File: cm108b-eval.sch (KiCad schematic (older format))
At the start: 42 parts, among them IC1 CM108B, J1 SPKR, J2 MIC, J3 RADIO_DATA, SW1 MUTE_REC, SW2 MUTE_PLAY, SW3 VOL_DN, SW4 VOL_UP

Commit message: Fix USB connector from A to micro-B
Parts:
- JP2: value USB_A -> USB_MICRO_B; symbol Connector:USB_A -> Connector:USB_B_Micro
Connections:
- net GND: now also JP2.5 (GND); no longer JP2.4 (GND)
- net at L2.2: now also JP2.6 (Shield); no longer JP2.5 (Shield)
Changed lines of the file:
@@
 $EndComp
 $Comp
-L Connector:USB_A JP2
+L Connector:USB_B_Micro JP2
 U 1 1 6057963A
 P 1350 2850
 F 0 "JP2" H 1407 3317 50  0000 C CNN
-F 1 "USB_A" H 1407 3226 50  0000 C CNN
+F 1 "USB_MICRO_B" H 1407 3226 50  0000 C CNN
 F 2 "Connector_USB:USB_Micro-B_Molex_47346-0001" H 1500 2800 50  0001 C CNN
 F 3 "https://www.mouser.com/datasheet/2/276/0473460001_IO_CONNECTORS-229243.pdf" H 1500 2800 50  0001 C CNN

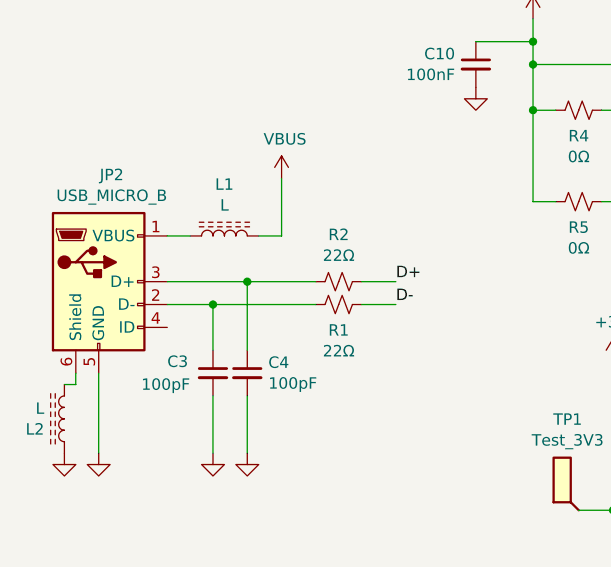
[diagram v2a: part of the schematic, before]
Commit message: Update micro USB part, and clean up libraries
The Molex micro USB is nearly impossible to hand solder, so I'm moving to the CUI
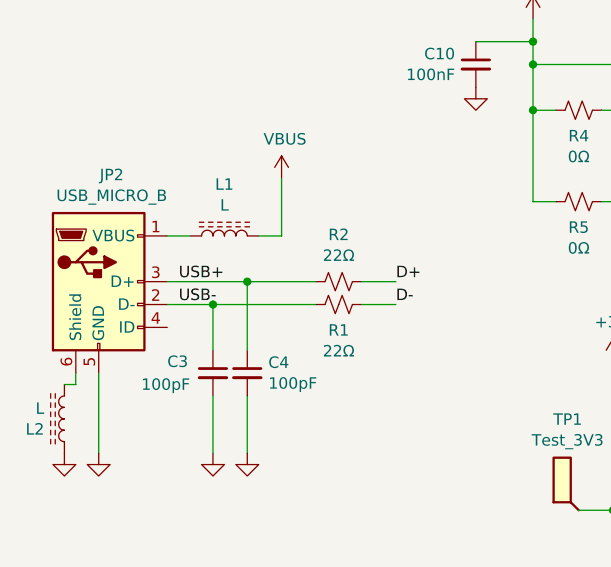
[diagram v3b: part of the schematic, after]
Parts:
- JP2: footprint Connector_USB:USB_Micro-B_Molex_47346-0001 -> CUI:UJ2-MIBH-4-SMT; Price 0.95 -> 0.79; Vendor Part # 538-47346-0001 -> 490-UJ2-MIBH-4-SMT
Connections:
- net USB-: now reaches C3.1, JP2.2 (D-), R1.2
- net USB+: now reaches C4.1, JP2.3 (D+), R2.2
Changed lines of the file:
@@
 Sheet 1 1
 Title "CM108B Evaluation Board"
-Date "2021-04-05"
-Rev "3"
+Date "2021-04-14"
+Rev "4"
 Comp "Chris Keller"
 Comment1 ""
@@
 NoConn ~ 4050 5150
 $Comp
-L power:GND #PWR?
+L power:GND #PWR0102
 U 1 1 605F61ED
 P 1350 3600
-F 0 "#PWR?" H 1350 3350 50  0001 C CNN
+F 0 "#PWR0102" H 1350 3350 50  0001 C CNN
 F 1 "GND" H 1355 3427 50  0001 C CNN
 F 2 "" H 1350 3600 50  0001 C CNN
@@
 F 0 "JP2" H 1407 3317 50  0000 C CNN
 F 1 "USB_MICRO_B" H 1407 3226 50  0000 C CNN
-F 2 "Connector_USB:USB_Micro-B_Molex_47346-0001" H 1500 2800 50  0001 C CNN
-F 3 "https://www.mouser.com/datasheet/2/276/0473460001_IO_CONNECTORS-229243.pdf" H 1500 2800 50  0001 C CNN
-F 4 "0.95" H 1407 3417 50  0001 C CNN "Price"
-F 5 "538-47346-0001" H 1407 3417 50  0001 C CNN "Vendor Part #"
+F 2 "CUI:UJ2-MIBH-4-SMT" H 1500 2800 50  0001 C CNN
+F 3 "https://www.mouser.com/datasheet/2/670/uj2_mibh_4_smt-1313358.pdf" H 1500 2800 50  0001 C CNN
+F 4 "0.79" H 1407 3417 50  0001 C CNN "Price"
+F 5 "490-UJ2-MIBH-4-SMT" H 1407 3417 50  0001 C CNN "Vendor Part #"
 F 6 "Mouser" H 1407 3417 50  0001 C CNN "Vendor"
 	1    1350 2850
@@
 Wire Wire Line
 	1250 3300 1200 3300
+Text Label 1700 2850 0    50   ~ 0
+USB+
+Text Label 1700 2950 0    50   ~ 0
+USB-
 $EndSCHEMATC

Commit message: Update BOM
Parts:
- R4: Vendor Part # 661-RK73Z2ETTD -> 660-RK73Z2ETTD
- R5: Vendor Part # 662-RK73Z2ETTD -> 660-RK73Z2ETTD
- R6: Vendor Part # 663-RK73Z2ETTD -> 660-RK73Z2ETTD
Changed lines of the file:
@@
 F 3 "https://www.mouser.com/datasheet/2/219/RK73Z-1825387.pdf" H 3450 2100 50  0001 C CNN
 F 4 "0.14" H 3563 2200 50  0001 C CNN "Price"
-F 5 "661-RK73Z2ETTD" H 3563 2200 50  0001 C CNN "Vendor Part #"
+F 5 "660-RK73Z2ETTD" H 3563 2200 50  0001 C CNN "Vendor Part #"
 F 6 "Mouser" H 3563 2200 50  0001 C CNN "Vendor"
 	1    3450 2100
@@
 F 3 "https://www.mouser.com/datasheet/2/219/RK73Z-1825387.pdf" H 3450 2500 50  0001 C CNN
 F 4 "0.14" H 3563 2600 50  0001 C CNN "Price"
-F 5 "662-RK73Z2ETTD" H 3563 2600 50  0001 C CNN "Vendor Part #"
+F 5 "660-RK73Z2ETTD" H 3563 2600 50  0001 C CNN "Vendor Part #"
 F 6 "Mouser" H 3563 2600 50  0001 C CNN "Vendor"
 	1    3450 2500
@@
 F 3 "https://www.mouser.com/datasheet/2/219/RK73Z-1825387.pdf" H 8550 3250 50  0001 C CNN
 F 4 "0.14" H 8663 3350 50  0001 C CNN "Price"
-F 5 "663-RK73Z2ETTD" H 8663 3350 50  0001 C CNN "Vendor Part #"
+F 5 "660-RK73Z2ETTD" H 8663 3350 50  0001 C CNN "Vendor Part #"
 F 6 "Mouser" H 8663 3350 50  0001 C CNN "Vendor"
 	1    8550 3250

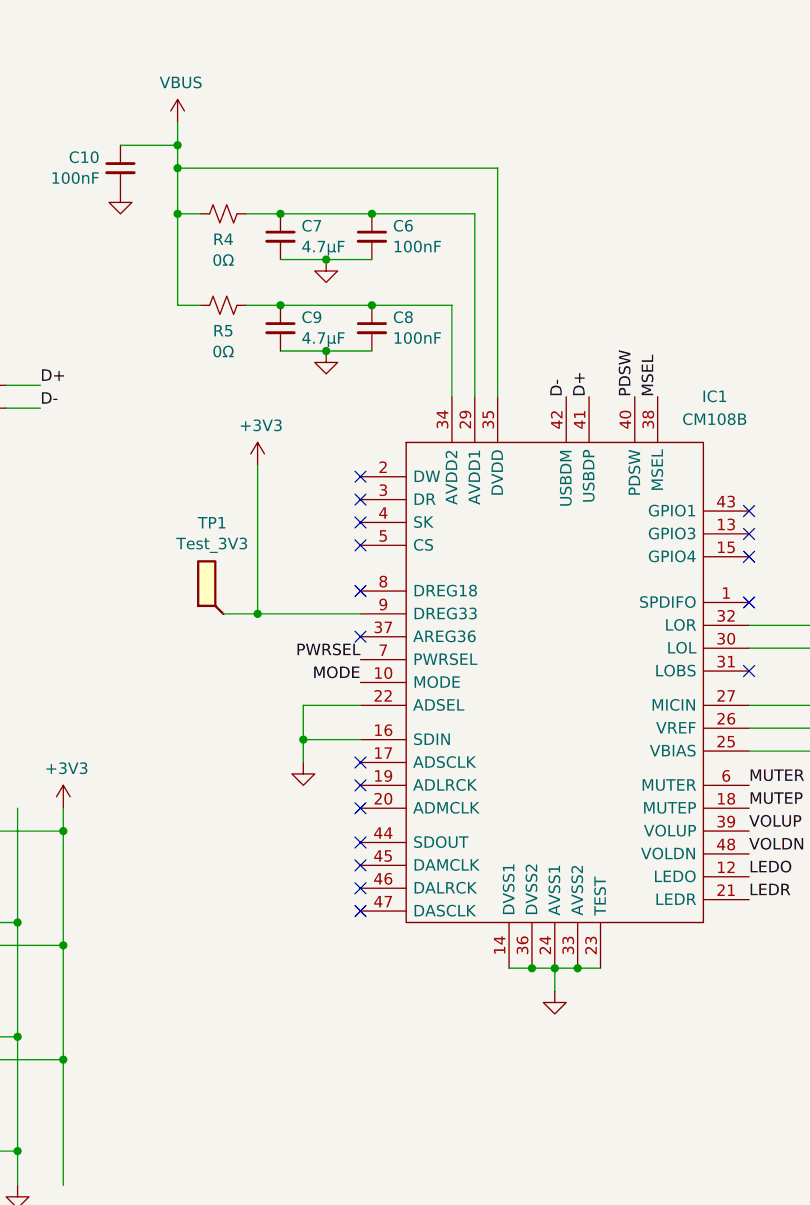
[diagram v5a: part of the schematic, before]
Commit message: Add more test points
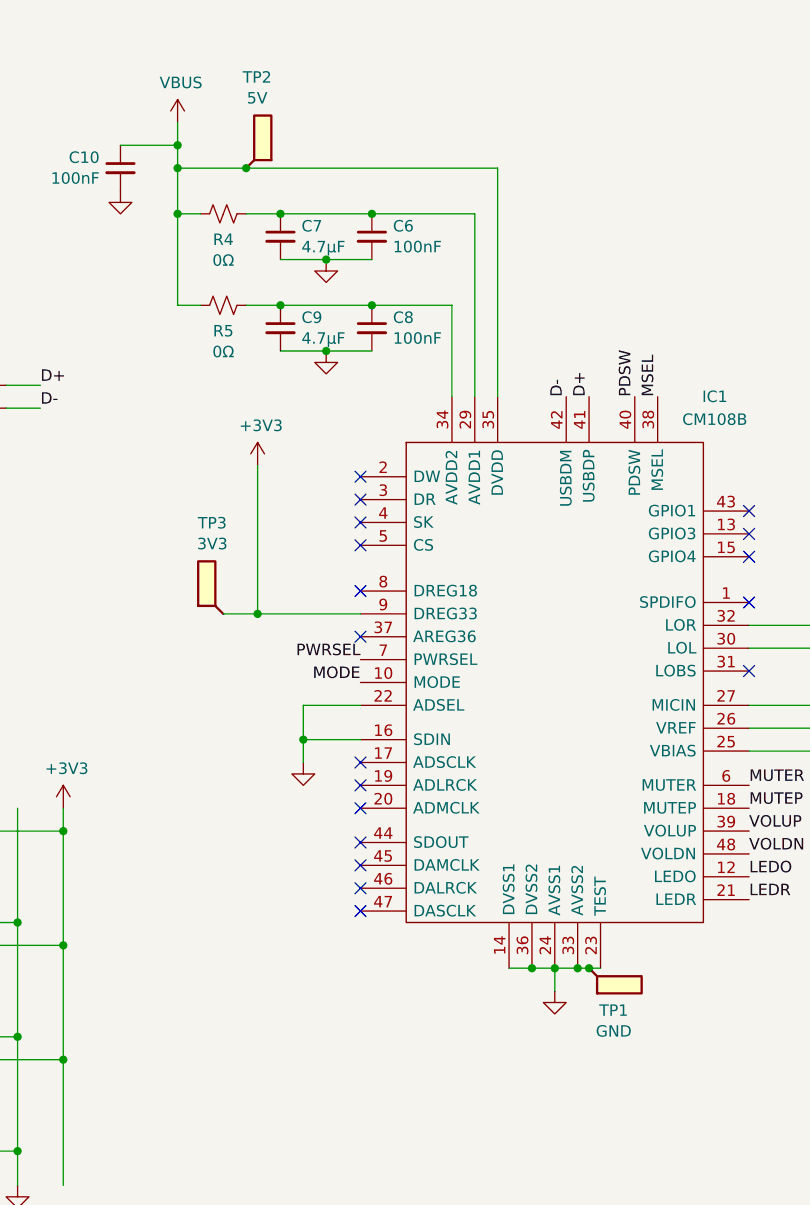
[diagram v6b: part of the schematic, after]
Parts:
- added TP1: GND, TestPoint:TestPoint_Pad_D2.0mm, symbol Connector:TestPoint_Flag
- added TP2: 5V, TestPoint:TestPoint_Pad_D1.0mm, symbol Connector:TestPoint_Flag
- C50, C51: footprint 293D477X9010E2TE3:CAPPM7343X430N -> Vishay:CAPPM7343X430N
- TP3: renamed from TP1; value Test_3V3 -> 3V3
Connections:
- net GND: now also TP1.1
- net VBUS: now also TP2.1
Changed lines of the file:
@@
 $EndComp
 $Comp
-L Connector:TestPoint_Flag TP1
+L Connector:TestPoint_Flag TP3
 U 1 1 605AD28D
 P 3450 3850
-F 0 "TP1" V 3847 3898 50  0000 C CNN
-F 1 "Test_3V3" V 3756 3898 50  0000 C CNN
+F 0 "TP3" V 3847 3898 50  0000 C CNN
+F 1 "3V3" V 3756 3898 50  0000 C CNN
 F 2 "TestPoint:TestPoint_Pad_D1.0mm" H 3650 3850 50  0001 C CNN
 F 3 "-" H 3650 3850 50  0001 C CNN
@@
 F 0 "C50" V 6855 3900 50  0000 C CNN
 F 1 "470μF" V 6764 3900 50  0000 C CNN
-F 2 "293D477X9010E2TE3:CAPPM7343X430N" H 6638 3750 50  0001 C CNN
+F 2 "Vishay:CAPPM7343X430N" H 6638 3750 50  0001 C CNN
 F 3 "https://www.mouser.com/datasheet/2/427/293d-1763499.pdf" H 6600 3900 50  0001 C CNN
 F 4 "1.3" H 6855 4000 50  0001 C CNN "Price"
@@
 F 0 "C51" V 7150 4000 50  0000 C CNN
 F 1 "470μF" V 7050 4000 50  0000 C CNN
-F 2 "293D477X9010E2TE3:CAPPM7343X430N" H 6938 3850 50  0001 C CNN
+F 2 "Vishay:CAPPM7343X430N" H 6938 3850 50  0001 C CNN
 F 3 "https://www.mouser.com/datasheet/2/427/293d-1763499.pdf" H 6900 4000 50  0001 C CNN
 F 4 "1.3" H 7150 4100 50  0001 C CNN "Price"
@@
 	4900 5400 5000 5400
 Wire Wire Line
-	5000 5400 5100 5400
+	5000 5400 5050 5400
 Wire Wire Line
 	4900 5400 4900 5500
@@
 	6950 4350 7000 4350
 Wire Wire Line
-	3250 1900 4650 1900
+	3250 1900 3550 1900
 Wire Wire Line
 	8900 5150 8700 5150
@@
 Text Label 1700 2950 0    50   ~ 0
 USB-
+$Comp
+L Connector:TestPoint_Flag TP2
+U 1 1 607EBAE2
+P 3550 1900
+F 0 "TP2" V 3947 1948 50  0000 C CNN
+F 1 "5V" V 3856 1948 50  0000 C CNN
+F 2 "TestPoint:TestPoint_Pad_D1.0mm" H 3750 1900 50  0001 C CNN
+F 3 "-" H 3750 1900 50  0001 C CNN
+F 4 "0" H 3947 2048 50  0001 C CNN "Price"
+F 5 "-" H 3947 2048 50  0001 C CNN "Vendor Part #"
+F 6 "-" H 3947 2048 50  0001 C CNN "Vendor"
+	1    3550 1900
+	0    1    -1   0
+$EndComp
+Connection ~ 3550 1900
+Wire Wire Line
+	3550 1900 4650 1900
+$Comp
+L Connector:TestPoint_Flag TP1
+U 1 1 607ECE47
+P 5050 5400
+F 0 "TP1" H 5158 5585 50  0000 C CNN
+F 1 "GND" H 5158 5676 50  0000 C CNN
+F 2 "TestPoint:TestPoint_Pad_D2.0mm" H 5250 5400 50  0001 C CNN
+F 3 "-" H 5250 5400 50  0001 C CNN
+F 4 "0" H 5447 5548 50  0001 C CNN "Price"
+F 5 "-" H 5447 5548 50  0001 C CNN "Vendor Part #"
+F 6 "-" H 5447 5548 50  0001 C CNN "Vendor"
+	1    5050 5400
+	1    0    0    1
+$EndComp
+Connection ~ 5050 5400
+Wire Wire Line
+	5050 5400 5100 5400
 $EndSCHEMATC

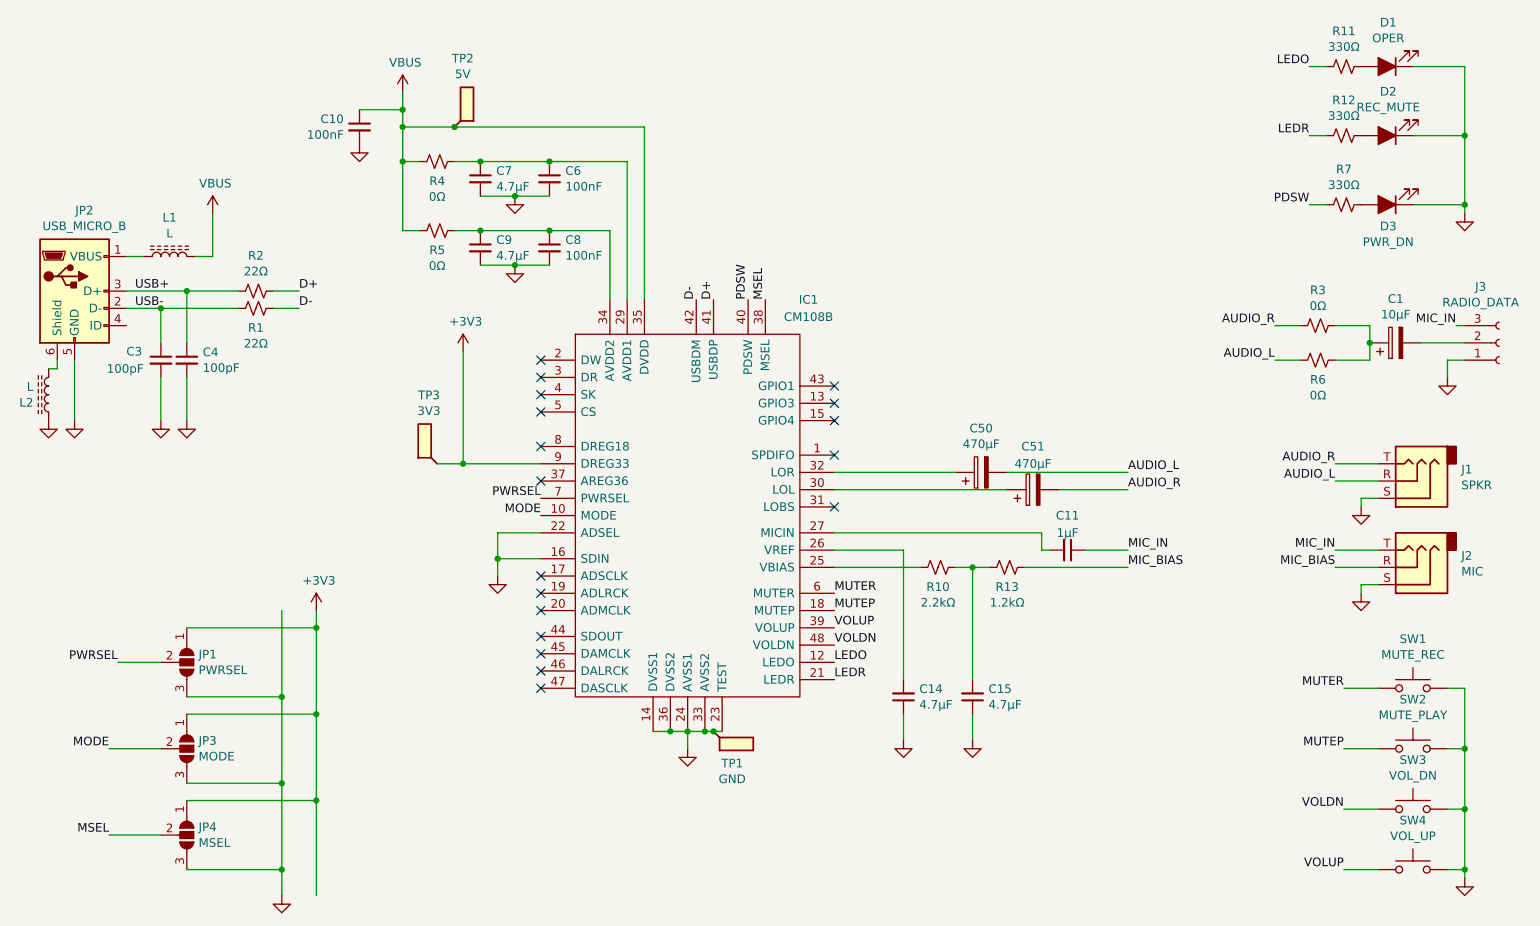
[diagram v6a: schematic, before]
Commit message: Move 5V test point to directly off USB
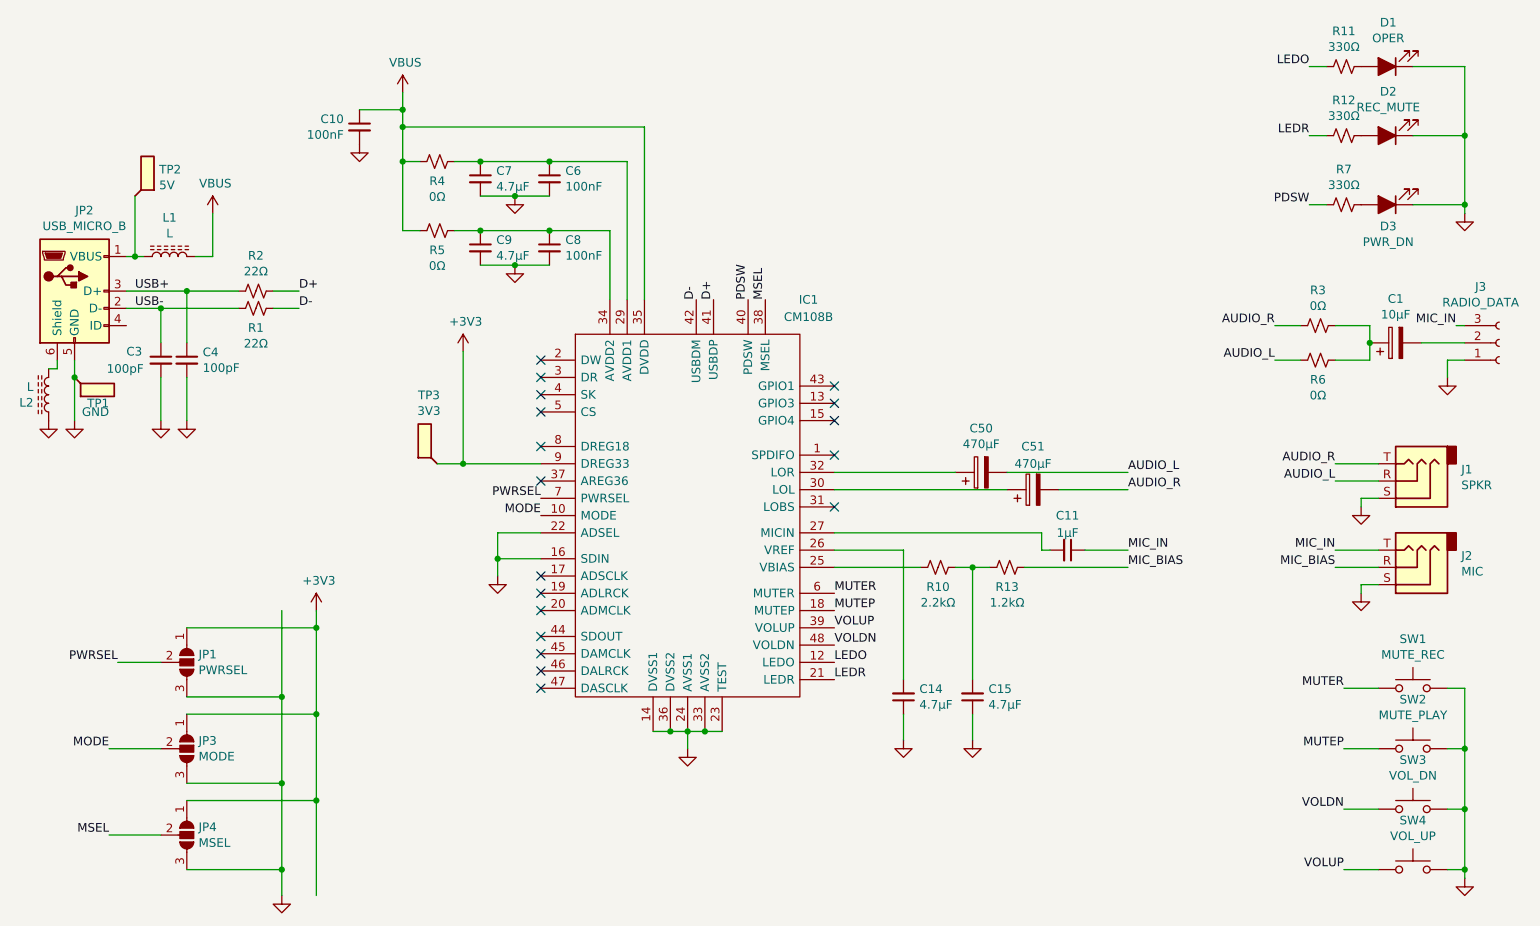
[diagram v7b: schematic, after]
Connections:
- net VBUS: no longer TP2.1
- net at JP2.1 (VBUS), L1.1: now also TP2.1
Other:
- moved on the sheet: TP1, TP2
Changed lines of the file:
@@
-$EndComp
-$Comp
-L Device:L_Core_Ferrite L1
-U 1 1 6059B333
-P 1900 2650
-F 0 "L1" V 2125 2650 50  0000 C CNN
-F 1 "L" V 2034 2650 50  0000 C CNN
-F 2 "Inductor_SMD:L_1210_3225Metric" H 1900 2650 50  0001 C CNN
-F 3 "https://www.mouser.com/datasheet/2/336/W719-1480588.pdf" H 1900 2650 50  0001 C CNN
-F 4 "0.92" H 2125 2750 50  0001 C CNN "Price"
-F 5 "673-PE1210CCMC161STS" H 2125 2750 50  0001 C CNN "Vendor Part #"
-F 6 "Mouser" H 2125 2750 50  0001 C CNN "Vendor"
-	1    1900 2650
-	0    -1   -1   0
 $EndComp
 $Comp
@@
 	4900 5400 5000 5400
 Wire Wire Line
-	5000 5400 5050 5400
-Wire Wire Line
 	4900 5400 4900 5500
 Wire Wire Line
@@
 	2500 2950 2650 2950
 Wire Wire Line
-	1650 2650 1750 2650
-Wire Wire Line
 	1850 3150 1850 2950
 Wire Wire Line
@@
 	8650 3250 8850 3250
 Wire Wire Line
-	2050 2650 2150 2650
-Wire Wire Line
 	2150 2650 2150 2400
 Wire Wire Line
@@
 Wire Wire Line
 	6950 4350 7000 4350
-Wire Wire Line
-	3250 1900 3550 1900
 Wire Wire Line
 	8900 5150 8700 5150
@@
 $EndComp
 Wire Wire Line
-	1350 3250 1350 3600
+	1350 3250 1350 3350
 Wire Wire Line
 	1250 3250 1250 3300
@@
 L Connector:TestPoint_Flag TP2
 U 1 1 607EBAE2
-P 3550 1900
-F 0 "TP2" V 3947 1948 50  0000 C CNN
-F 1 "5V" V 3856 1948 50  0000 C CNN
-F 2 "TestPoint:TestPoint_Pad_D1.0mm" H 3750 1900 50  0001 C CNN
-F 3 "-" H 3750 1900 50  0001 C CNN
-F 4 "0" H 3947 2048 50  0001 C CNN "Price"
-F 5 "-" H 3947 2048 50  0001 C CNN "Vendor Part #"
-F 6 "-" H 3947 2048 50  0001 C CNN "Vendor"
-	1    3550 1900
+P 1700 2300
+F 0 "TP2" V 1854 2440 50  0000 L CNN
+F 1 "5V" V 1763 2440 50  0000 L CNN
+F 2 "TestPoint:TestPoint_Pad_D1.0mm" H 1900 2300 50  0001 C CNN
+F 3 "-" H 1900 2300 50  0001 C CNN
+F 4 "0" H 2097 2448 50  0001 C CNN "Price"
+F 5 "-" H 2097 2448 50  0001 C CNN "Vendor Part #"
+F 6 "-" H 2097 2448 50  0001 C CNN "Vendor"
+	1    1700 2300
 	0    1    -1   0
 $EndComp
-Connection ~ 3550 1900
-Wire Wire Line
-	3550 1900 4650 1900
 $Comp
 L Connector:TestPoint_Flag TP1
 U 1 1 607ECE47
-P 5050 5400
-F 0 "TP1" H 5158 5585 50  0000 C CNN
-F 1 "GND" H 5158 5676 50  0000 C CNN
-F 2 "TestPoint:TestPoint_Pad_D2.0mm" H 5250 5400 50  0001 C CNN
-F 3 "-" H 5250 5400 50  0001 C CNN
-F 4 "0" H 5447 5548 50  0001 C CNN "Price"
-F 5 "-" H 5447 5548 50  0001 C CNN "Vendor Part #"
-F 6 "-" H 5447 5548 50  0001 C CNN "Vendor"
-	1    5050 5400
+P 1350 3350
+F 0 "TP1" H 1550 3500 50  0000 R CNN
+F 1 "GND" H 1550 3550 50  0000 R CNN
+F 2 "TestPoint:TestPoint_Pad_D2.0mm" H 1550 3350 50  0001 C CNN
+F 3 "-" H 1550 3350 50  0001 C CNN
+F 4 "0" H 1747 3498 50  0001 C CNN "Price"
+F 5 "-" H 1747 3498 50  0001 C CNN "Vendor Part #"
+F 6 "-" H 1747 3498 50  0001 C CNN "Vendor"
+	1    1350 3350
 	1    0    0    1
 $EndComp
-Connection ~ 5050 5400
-Wire Wire Line
-	5050 5400 5100 5400
+Wire Wire Line
+	3250 1900 4650 1900
+Wire Wire Line
+	2050 2650 2150 2650
+Wire Wire Line
+	1650 2650 1700 2650
+$Comp
+L Device:L_Core_Ferrite L1
+U 1 1 6059B333
+P 1900 2650
+F 0 "L1" V 2125 2650 50  0000 C CNN
+F 1 "L" V 2034 2650 50  0000 C CNN
+F 2 "Inductor_SMD:L_1210_3225Metric" H 1900 2650 50  0001 C CNN
+F 3 "https://www.mouser.com/datasheet/2/336/W719-1480588.pdf" H 1900 2650 50  0001 C CNN
+F 4 "0.92" H 2125 2750 50  0001 C CNN "Price"
+F 5 "673-PE1210CCMC161STS" H 2125 2750 50  0001 C CNN "Vendor Part #"
+F 6 "Mouser" H 2125 2750 50  0001 C CNN "Vendor"
+	1    1900 2650
+	0    -1   -1   0
+$EndComp
+Wire Wire Line
+	1700 2300 1700 2650
+Connection ~ 1700 2650
+Wire Wire Line
+	1700 2650 1750 2650
+Connection ~ 1350 3350
+Wire Wire Line
+	1350 3350 1350 3600
+Wire Wire Line
+	5000 5400 5100 5400
 $EndSCHEMATC
